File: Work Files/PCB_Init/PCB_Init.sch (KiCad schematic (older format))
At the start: 35 parts

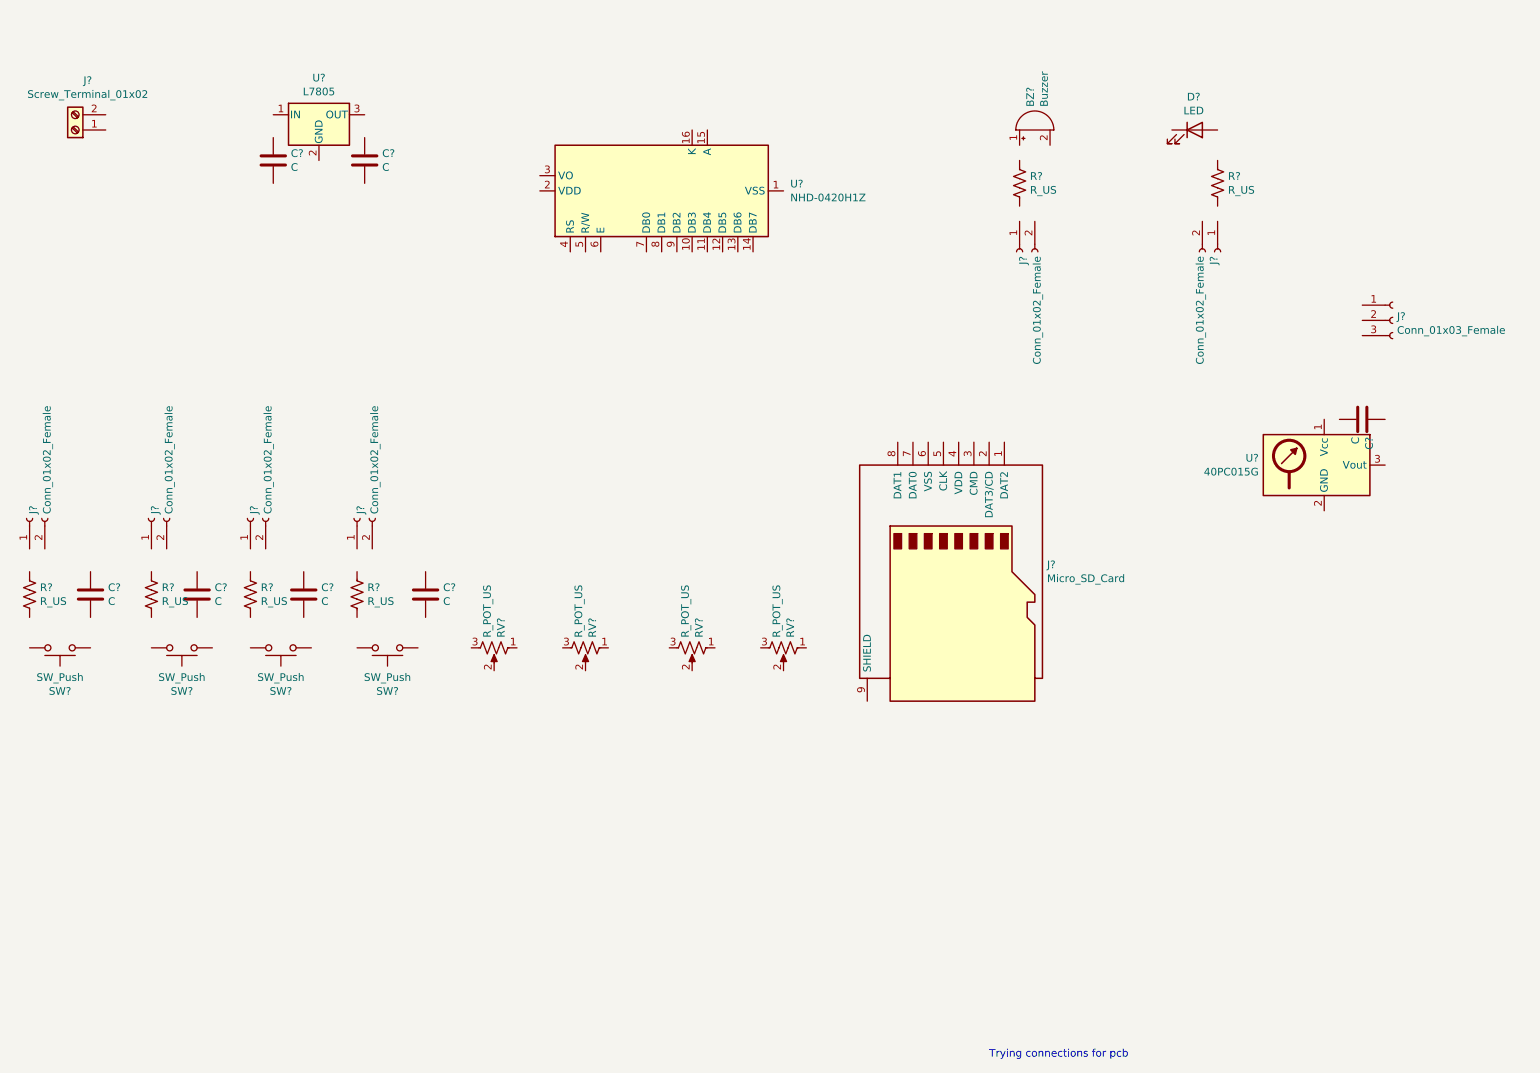
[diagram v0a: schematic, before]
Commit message: Wired connections in Eeschema, would be changed in later development
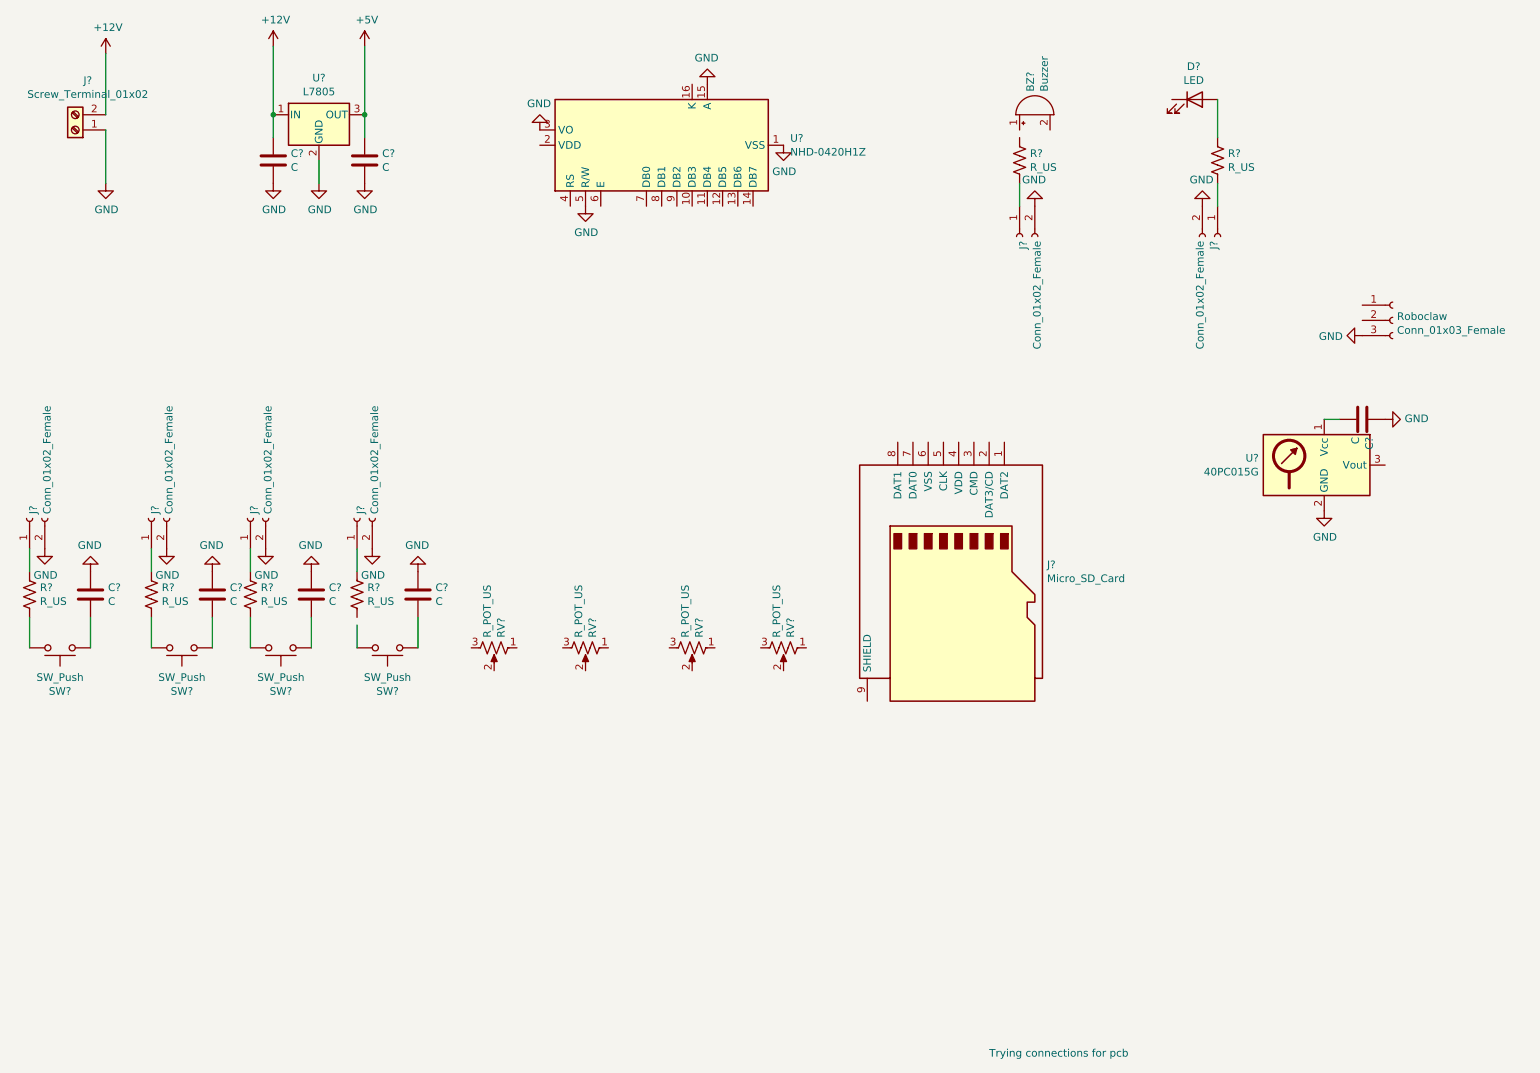
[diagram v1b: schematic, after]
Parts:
- gave numbers to parts that had none: 1
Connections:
- net labels added: +12V, +5V, GND
- wire segments 0 -> 23
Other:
- moved on the sheet: BZ?, C?, D?, J?, R?, U?
